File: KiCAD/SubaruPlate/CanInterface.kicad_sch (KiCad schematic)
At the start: 10 parts, among them J1 DF51A-4P-2DSA, U3 MCP2515-xSO, U4 MCP2562-E-SN, Y1 8MHz

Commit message: SubaruPlateを更新
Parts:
- added C4, C5: 0.1uF, Capacitor_SMD:C_0603_1608Metric_Pad1.08x0.95mm_HandSolder, symbol Device:C
- R4: footprint (none) -> Resistor_SMD:R_0603_1608Metric_Pad0.98x0.95mm_HandSolder
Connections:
- net +3.3V: now also C4.2, C5.2
- net GND: now also C4.1, C5.1
- net SPI_SI renamed SPI_MOSI
- net SPI_SO renamed SPI_MISO
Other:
- moved on the sheet: C3, C6, C7, JP1, R4, R6, U3, U4, Y1

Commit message: 後は最終確認
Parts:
- removed JP1: Jumper_2_Open, Jumper:SolderJumper-2_P1.3mm_Open_TrianglePad1.0x1.5mm, symbol Jumper:Jumper_2_Open
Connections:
- net CAN_H: now also R6.2
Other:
- moved on the sheet: R6
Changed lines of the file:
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@@
 	)
 	(junction
-		(at 177.8 60.96)
-		(diameter 0)
-		(color 0 0 0 0)
-	)
-	(junction
-		(at 177.8 33.02)
+		(at 177.8 54.61)
 		(diameter 0)
 		(color 0 0 0 0)
@@
 		(color 0 0 0 0)
 	)
+	(junction
+		(at 177.8 41.91)
+		(diameter 0)
+		(color 0 0 0 0)
+	)
 	(no_connect
 		(at 85.09 72.39)
@@
 	(wire
 		(pts
+			(xy 177.8 41.91) (xy 177.8 44.45)
+		)
+		(stroke
+			(width 0)
+			(type default)
+		)
+	)
+	(wire
+		(pts
 			(xy 69.85 38.1) (xy 69.85 46.99)
 		)
@@
 	(wire
 		(pts
-			(xy 177.8 45.72) (xy 177.8 50.8)
-		)
-		(stroke
-			(width 0)
-			(type default)
-		)
-	)
-	(wire
-		(pts
 			(xy 60.96 115.57) (xy 71.12 115.57)
 		)
@@
 	(wire
 		(pts
-			(xy 177.8 33.02) (xy 182.88 33.02)
+			(xy 177.8 41.91) (xy 182.88 41.91)
 		)
 		(stroke
@@
 	(wire
 		(pts
-			(xy 162.56 33.02) (xy 162.56 45.72)
+			(xy 162.56 41.91) (xy 162.56 45.72)
 		)
 		(stroke
@@
 	(wire
 		(pts
-			(xy 177.8 60.96) (xy 162.56 60.96)
+			(xy 177.8 54.61) (xy 162.56 54.61)
 		)
 		(stroke
@@
 	(wire
 		(pts
-			(xy 162.56 33.02) (xy 177.8 33.02)
+			(xy 162.56 41.91) (xy 177.8 41.91)
 		)
 		(stroke
@@
 	(wire
 		(pts
-			(xy 182.88 60.96) (xy 177.8 60.96)
+			(xy 182.88 54.61) (xy 177.8 54.61)
 		)
 		(stroke
@@
 	(wire
 		(pts
-			(xy 177.8 33.02) (xy 177.8 35.56)
-		)
-		(stroke
-			(width 0)
-			(type default)
-		)
-	)
-	(wire
-		(pts
 			(xy 97.79 82.55) (xy 97.79 80.01)
 		)
@@
 	(wire
 		(pts
-			(xy 162.56 60.96) (xy 162.56 50.8)
+			(xy 162.56 54.61) (xy 162.56 50.8)
 		)
 		(stroke
@@
 	(wire
 		(pts
-			(xy 177.8 58.42) (xy 177.8 60.96)
+			(xy 177.8 52.07) (xy 177.8 54.61)
 		)
 		(stroke
@@
 	(global_label "CAN_L"
 		(shape bidirectional)
-		(at 182.88 60.96 0)
+		(at 182.88 54.61 0)
 		(fields_autoplaced yes)
 		(effects
@@
 		)
 		(property "Intersheetrefs" "${INTERSHEET_REFS}"
-			(at 192.6613 60.96 0)
+			(at 192.6613 54.61 0)
 			(effects
 				(font
@@
 	(global_label "CAN_H"
 		(shape bidirectional)
-		(at 182.88 33.02 0)
+		(at 182.88 41.91 0)
 		(fields_autoplaced yes)
 		(effects
@@
 		)
 		(property "Intersheetrefs" "${INTERSHEET_REFS}"
-			(at 192.9637 33.02 0)
+			(at 192.9637 41.91 0)
 			(effects
 				(font
@@
 	(symbol
 		(lib_id "Device:R")
-		(at 177.8 54.61 180)
+		(at 177.8 48.26 180)
 		(unit 1)
 		(exclude_from_sim no)
@@
 		(fields_autoplaced yes)
 		(property "Reference" "R6"
-			(at 180.34 53.3399 0)
+			(at 180.34 46.9899 0)
 			(effects
 				(font
@@
 		)
 		(property "Value" "120"
-			(at 180.34 55.8799 0)
+			(at 180.34 49.5299 0)
 			(effects
 				(font
@@
 		)
 		(property "Footprint" "Resistor_SMD:R_0603_1608Metric_Pad0.98x0.95mm_HandSolder"
-			(at 179.578 54.61 90)
+			(at 179.578 48.26 90)
 			(effects
 				(font
@@
 		)
 		(property "Datasheet" "~"
-			(at 177.8 54.61 0)
+			(at 177.8 48.26 0)
 			(effects
 				(font
@@
 		)
 		(property "Description" "Resistor"
-			(at 177.8 54.61 0)
+			(at 177.8 48.26 0)
 			(effects
 				(font
@@
 					(unit 1)
 				)
-			)
-		)
-	)
-	(symbol
-		(lib_id "Jumper:Jumper_2_Open")
-		(at 177.8 40.64 270)
-		(unit 1)
-		(exclude_from_sim no)
-		(in_bom yes)
-		(on_board yes)
-		(dnp no)
-		(fields_autoplaced yes)
-		(property "Reference" "JP1"
-			(at 180.34 39.3699 90)
-			(effects
-				(font
-					(size 1.27 1.27)
-				)
-				(justify left)
-			)
-		)
-		(property "Value" "Jumper_2_Open"
-			(at 180.34 41.9099 90)
-			(effects
-				(font
-					(size 1.27 1.27)
-				)
-				(justify left)
-			)
-		)
-		(property "Footprint" "Jumper:SolderJumper-2_P1.3mm_Open_TrianglePad1.0x1.5mm"
-			(at 177.8 40.64 0)
-			(effects
-				(font
-					(size 1.27 1.27)
-				)
-				(hide yes)
-			)
-		)
-		(property "Datasheet" "~"
-			(at 177.8 40.64 0)
-			(effects
-				(font
-					(size 1.27 1.27)
-				)
-				(hide yes)
-			)
-		)
-		(property "Description" "Jumper, 2-pole, open"
-			(at 177.8 40.64 0)
-			(effects
-				(font
-					(size 1.27 1.27)
-				)
-				(hide yes)
-			)
-		)
-		(pin "2"
-		)
-		(pin "1"
-		)
-		(instances
-			(project ""
-				(path "/6c4aa1f5-c08b-4349-85f8-88bb399e711f/44ad5b2d-22cb-4ed2-bb54-706dcaaae99f"
-					(reference "JP1")
-					(unit 1)
-				)

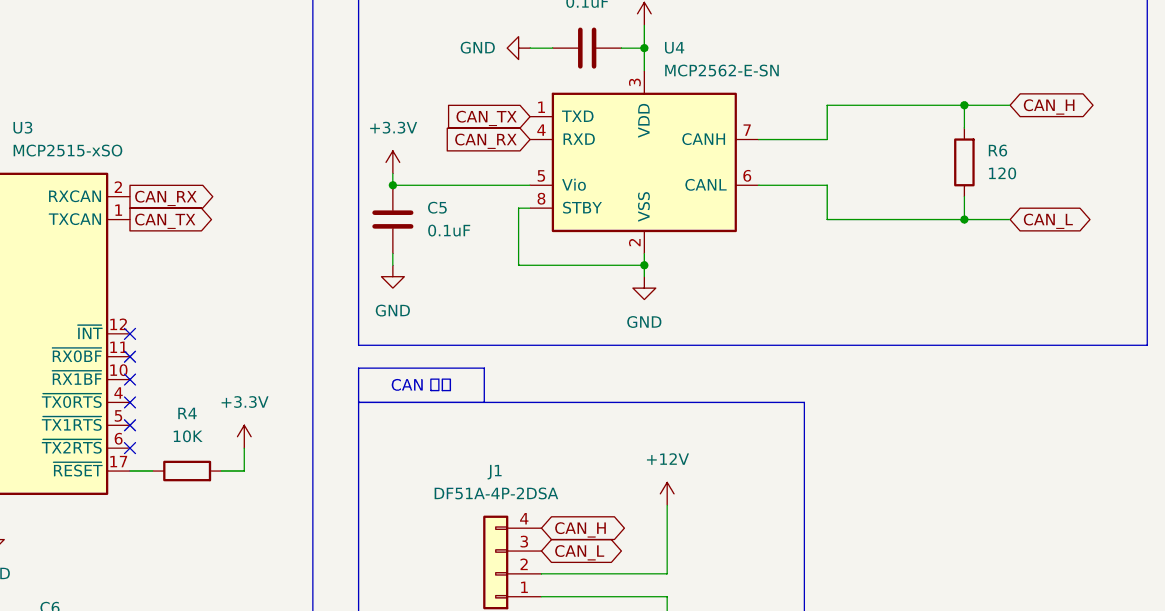
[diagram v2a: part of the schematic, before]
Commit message: 取付穴位置を変更
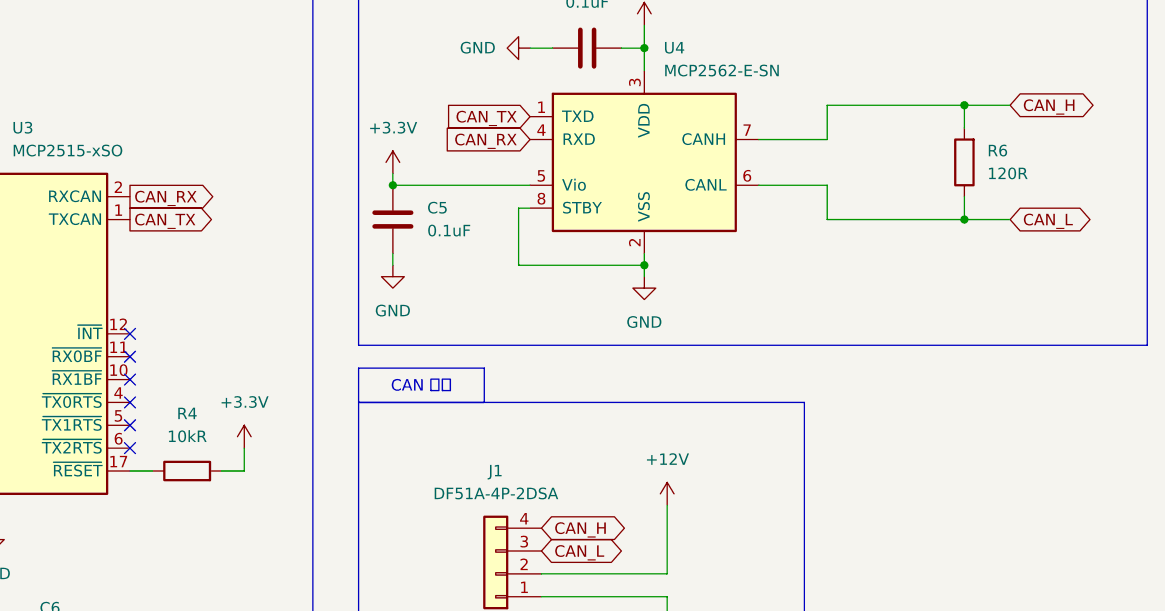
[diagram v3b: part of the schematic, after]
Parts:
- R4: value 10K -> 10kR
- R6: value 120 -> 120R
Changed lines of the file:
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@@
 			)
 		)
-		(property "Value" "120"
+		(property "Value" "120R"
 			(at 180.34 49.5299 0)
 			(effects
@@
 			)
 		)
-		(property "Value" "10K"
+		(property "Value" "10kR"
 			(at 91.44 78.74 90)
 			(effects
